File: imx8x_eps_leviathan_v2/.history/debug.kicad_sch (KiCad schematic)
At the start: 77 parts, among them U19 CAT93C66VI-GT3, U20 FT2232HL, U21 LP38693MP-ADJ/NOPB, U22 TXS0101DCKR, U23 TXS0101DCKR, Y1 12MHz

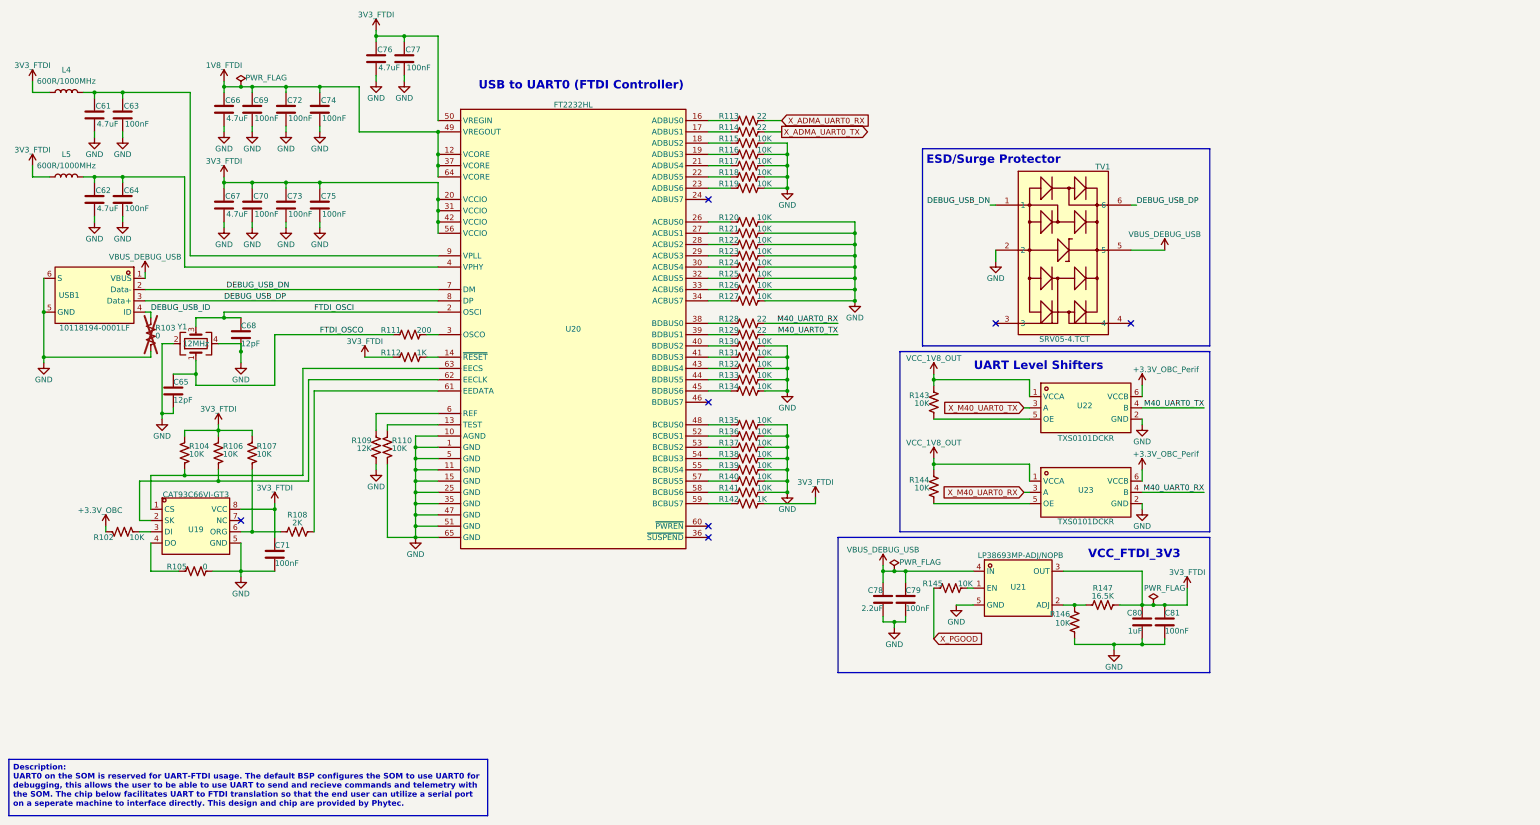
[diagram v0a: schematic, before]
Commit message: Goodies
Updated USB to USB C. Added Diodes for USB. Improved Layout. Ready for some routing.
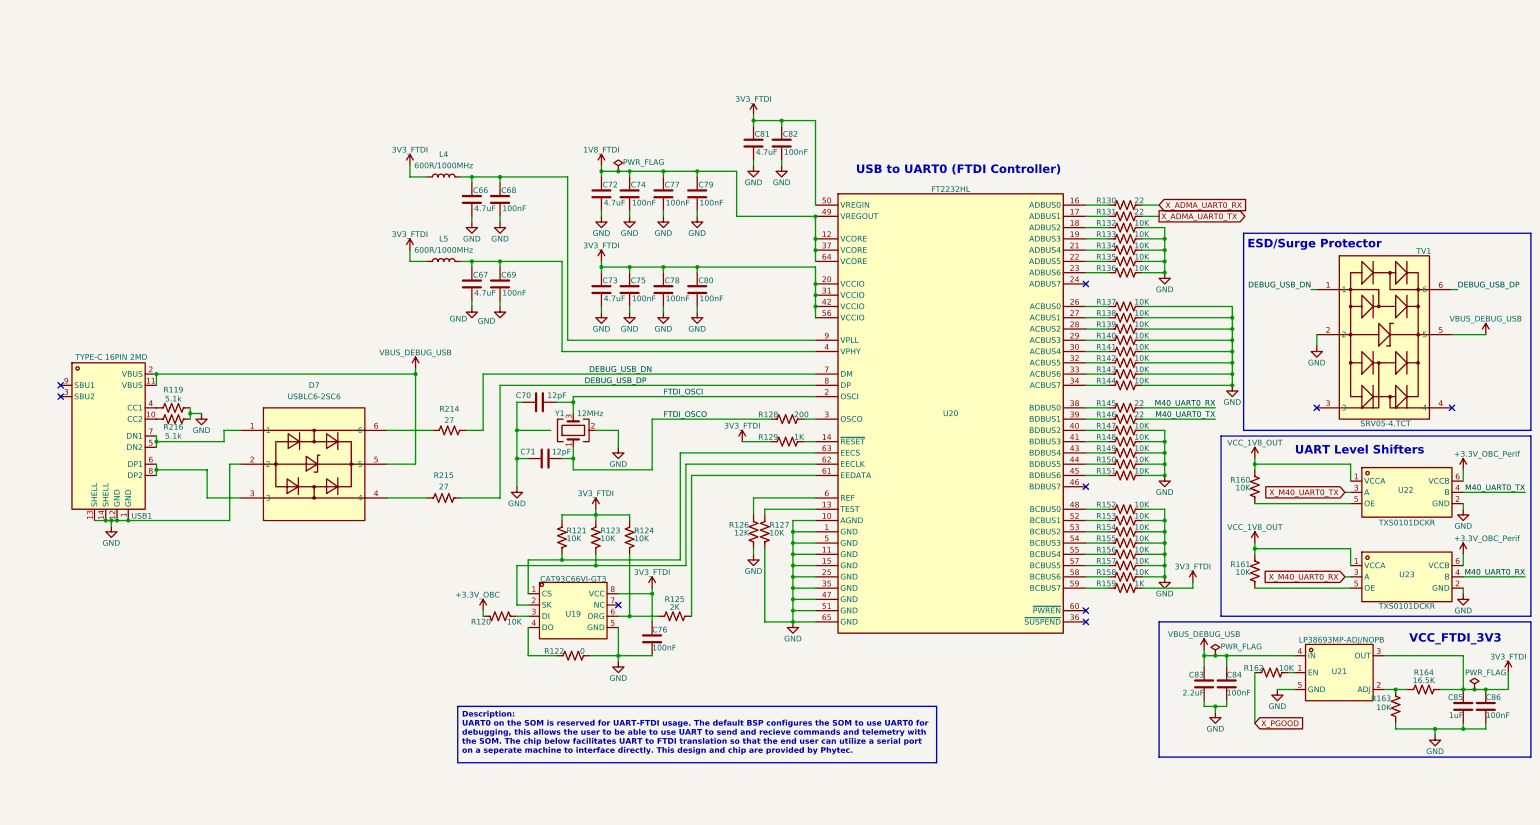
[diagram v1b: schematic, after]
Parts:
- removed C68: 12pF, EPS:C0402, symbol Device:C
- removed R103: 0, EPS:R0402, symbol Device:R_US
- removed USB1: 10118194-0001LF, imx8_carrier_board_footprints:MICRO-USB-SMD_10118194-0001LF, symbol imx8_carrier_board_symbol_library:10118194-0001LF
- added C70: 12pF, EPS:C0402, symbol Device:C
- added D7: USBLC6-2SC6, imx8_carrier_board_footprints:SOT-23-6_L2.9-W1.6-P0.95-LS2.8-BL, symbol imx8_carrier_board_symbol_library:USBLC6-2SC6
- added R119, R216: 5.1k, symbol Device:R_US
- added R214, R215: 27, symbol Device:R_US
- added USB1: TYPE-C 16PIN 2MD, imx8_carrier_board_footprints:USB-C-SMD_TYPE-C-6PIN-2MD-073, symbol imx8_carrier_board_symbol_library:TYPE-C16PIN2MD
- renumbered C61 to C66, C62 to C67, C63 to C68, C64 to C69, C65 to C71, C66 to C72, C67 to C73, C69 to C74, C70 to C75, C71 to C76, C72 to C77, C73 to C78, C74 to C79, C75 to C80, C76 to C81, C77 to C82, C78 to C83, C79 to C84, C80 to C85, C81 to C86, R102 to R120, R104 to R121, R105 to R122, R106 to R123, R107 to R124, R108 to R125, R109 to R126, R110 to R127, R111 to R128, R112 to R129, R113 to R130, R114 to R131, R115 to R132, R116 to R133, R117 to R134, R118 to R135, R119 to R136, R120 to R137, R121 to R138, R122 to R139, R123 to R140, R124 to R141, R125 to R142, R126 to R143, R127 to R144, R128 to R145, R129 to R146, R130 to R147, R131 to R148, R132 to R149, R133 to R150, R134 to R151, R135 to R152, R136 to R153, R137 to R154, R138 to R155, R139 to R156, R140 to R157, R141 to R158, R142 to R159, R143 to R160, R144 to R161, R145 to R162, R146 to R163, R147 to R164
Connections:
- net DEBUG_USB_DN: now also R214.2
- net DEBUG_USB_DP: now also R215.2
- net FTDI_OSCI: now also C70.1
- net FTDI_OSCO: now also C71.1; no longer C71.2
- net GND: now also C71.2, C70.2, D7.2, R119.2, R216.2, USB1.1 (GND), USB1.12 (GND), USB1.13 (SHELL), USB1.14 (SHELL); no longer C71.1
- net VBUS_DEBUG_USB: now also D7.5, USB1.11 (VBUS), USB1.2 (VBUS)
- new net: D7.1, USB1.5 (DN2), USB1.7 (DN1)
- new net: D7.3, USB1.6 (DP1), USB1.8 (DP2)
- new net: D7.4, R215.1
- new net: D7.6, R214.1
- new net: R119.1, USB1.4 (CC1)
- new net: R216.1, USB1.10 (CC2)
- no-connect marks 7 -> 9
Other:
- title: Leviathan V1 -> Leviathan V2
- moved on the sheet: C66, C67, C68, C69, C71, C72, C73, C74, C75, C76, C77, C78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

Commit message: Started routing
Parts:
- removed D7: USBLC6-2SC6, imx8_carrier_board_footprints:SOT-23-6_L2.9-W1.6-P0.95-LS2.8-BL, symbol imx8_carrier_board_symbol_library:USBLC6-2SC6
- removed Y1: 12MHz, imx8_carrier_board_footprints:CRYSTAL-SMD_4P-L3.2-W2.5-BL, symbol Device:Crystal_GND24
- added Y1: Crystal_GND24, symbol imx8_carrier_board_symbol_library:Crystal_GND24
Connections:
- net DEBUG_USB_DN: now also R214.1, USB1.5 (DN2), USB1.7 (DN1)
- net DEBUG_USB_DP: now also R215.1, USB1.6 (DP1), USB1.8 (DP2)
- net FTDI_OSCI: now also Y1.3
- net FTDI_OSCO: now also Y1.1
- net GND: now also Y1.2 (G), Y1.4 (G)
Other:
- moved on the sheet: R119, R214, R215, R216, USB1

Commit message: Added review page and starting to implement requested changes.
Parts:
- Y1: footprint (none) -> imx8_carrier_board_footprints:CRYSTAL-SMD_4P-L3.2-W2.5-BL
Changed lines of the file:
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@@
 			)
 		)
-		(property "Footprint" ""
+		(property "Footprint" "imx8_carrier_board_footprints:CRYSTAL-SMD_4P-L3.2-W2.5-BL"
 			(at 139.7 110.49 0)
 			(hide yes)
